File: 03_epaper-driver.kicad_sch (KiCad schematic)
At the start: 21 parts, among them J6 FFC2B28-24-G, Q4 BSS138

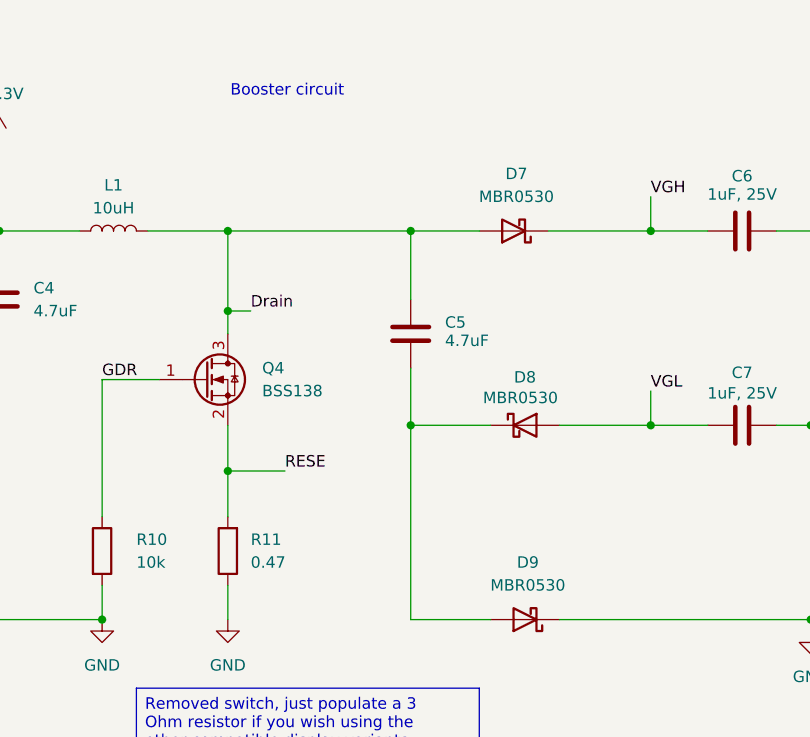
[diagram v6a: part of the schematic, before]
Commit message: Add an voltage bypass mode when USB-C is connected
When USB-C is connected, the device should be charging, but also powered,
without taking care of the on/off button's state.
Otherwise, flashing the device via USB-C would only be
possible as long as the button is pressed which makes the usage
experience a mess and flaky.
This uses p-MOSFETs to do the switch and
a) avoid a battery voltage going to the system when USB-C is connected
b) avoid powering having both, USB-C and Micro-USB active

TODO: This adds the basic idea, routing must be fixed!
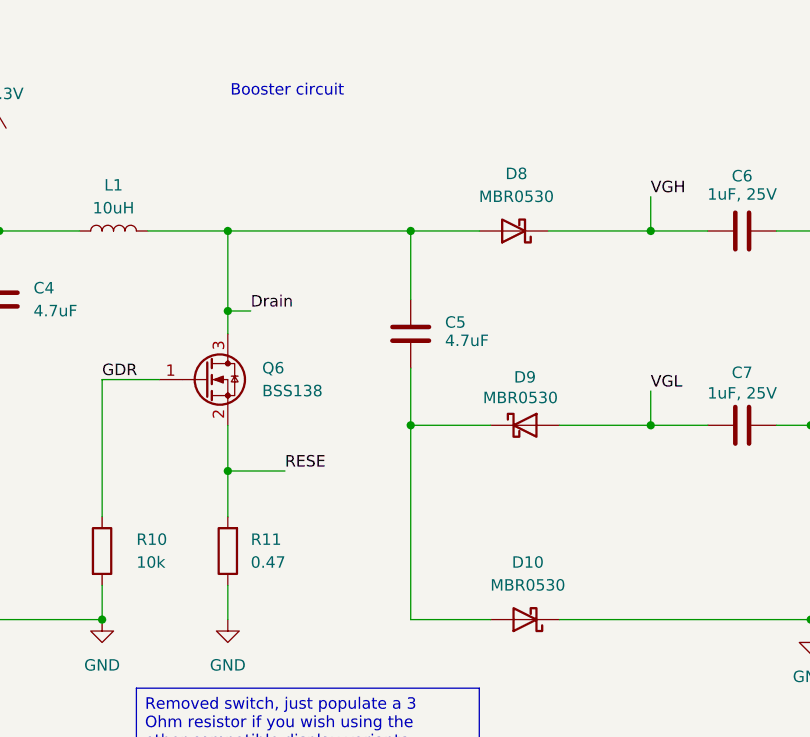
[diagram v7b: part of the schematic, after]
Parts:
- renumbered D9 to D10, D7 to D8, D8 to D9, Q4 to Q6
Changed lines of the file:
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@@
 		(dnp no)
 		(fields_autoplaced yes)
-		(property "Reference" "D7"
+		(property "Reference" "D8"
 			(at 95.5675 69.85 0)
 			(effects
@@
 			(project ""
 				(path "/ec954637-2a8b-4662-b4a1-f88107f11cb0/d006ff72-e176-4e99-8906-01d59b86077c"
-					(reference "D7")
+					(reference "D8")
 					(unit 1)
 				)
@@
 		(on_board yes)
 		(dnp no)
-		(property "Reference" "D8"
+		(property "Reference" "D9"
 			(at 96.52 92.456 0)
 			(effects
@@
 			(project ""
 				(path "/ec954637-2a8b-4662-b4a1-f88107f11cb0/d006ff72-e176-4e99-8906-01d59b86077c"
-					(reference "D8")
+					(reference "D9")
 					(unit 1)
 				)
@@
 		(dnp no)
 		(fields_autoplaced yes)
-		(property "Reference" "Q4"
+		(property "Reference" "Q6"
 			(at 67.31 91.4399 0)
 			(effects
@@
 			(project ""
 				(path "/ec954637-2a8b-4662-b4a1-f88107f11cb0/d006ff72-e176-4e99-8906-01d59b86077c"
-					(reference "Q4")
+					(reference "Q6")
 					(unit 1)
 				)
@@
 		(dnp no)
 		(fields_autoplaced yes)
-		(property "Reference" "D9"
+		(property "Reference" "D10"
 			(at 96.8375 113.03 0)
 			(effects
@@
 			(project ""
 				(path "/ec954637-2a8b-4662-b4a1-f88107f11cb0/d006ff72-e176-4e99-8906-01d59b86077c"
-					(reference "D9")
+					(reference "D10")
 					(unit 1)
 				)
